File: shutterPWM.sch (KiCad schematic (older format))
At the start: 25 parts, among them P11 2x3 header strip R/A, P12 2x3 header strip R/A, U2 DRV103, U3 DRV103, U4 MCP4728

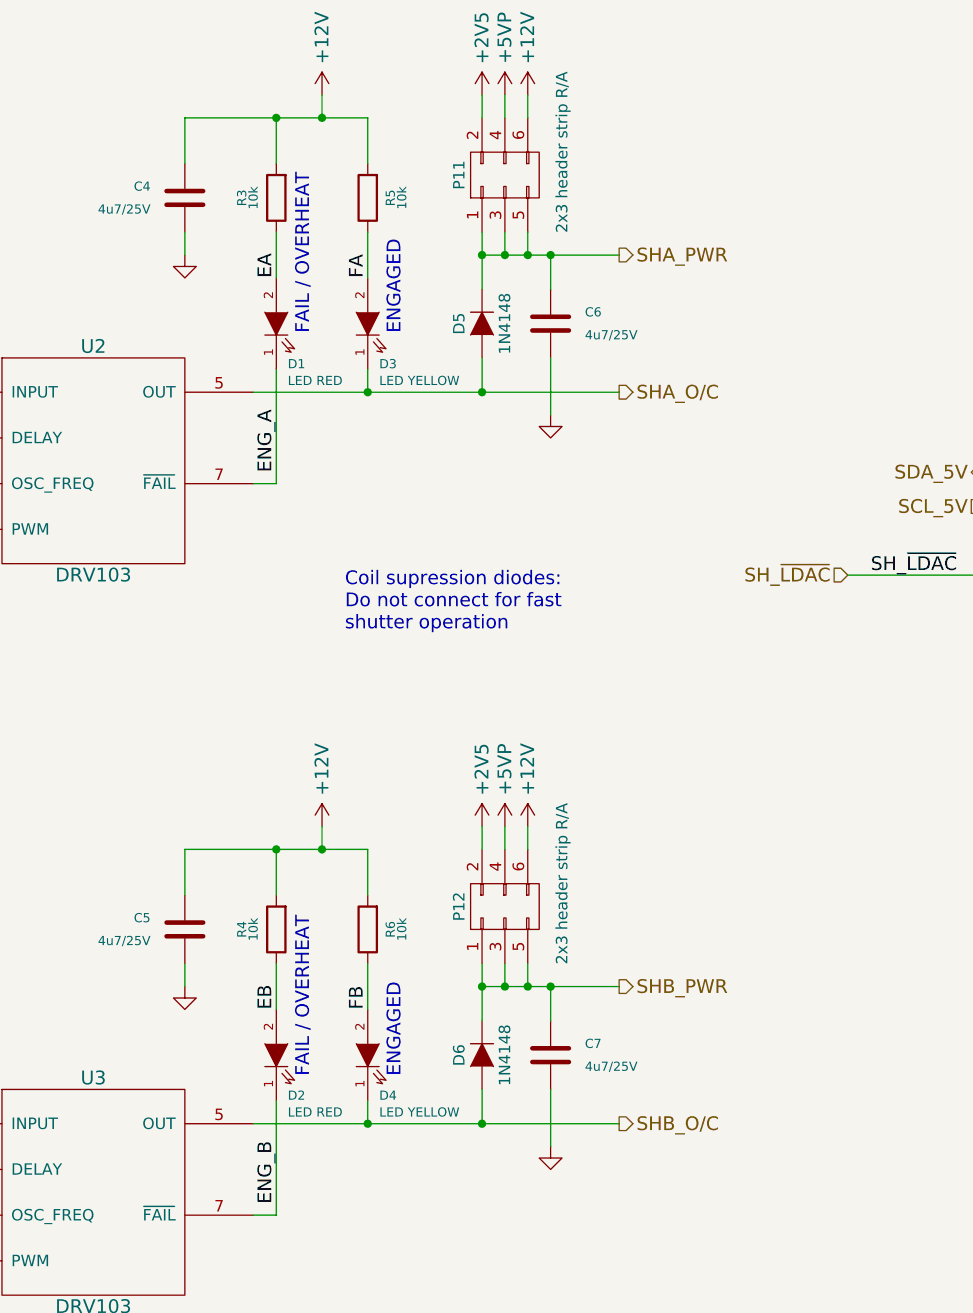
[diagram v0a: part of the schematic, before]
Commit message: Added better de-bouncing diode description
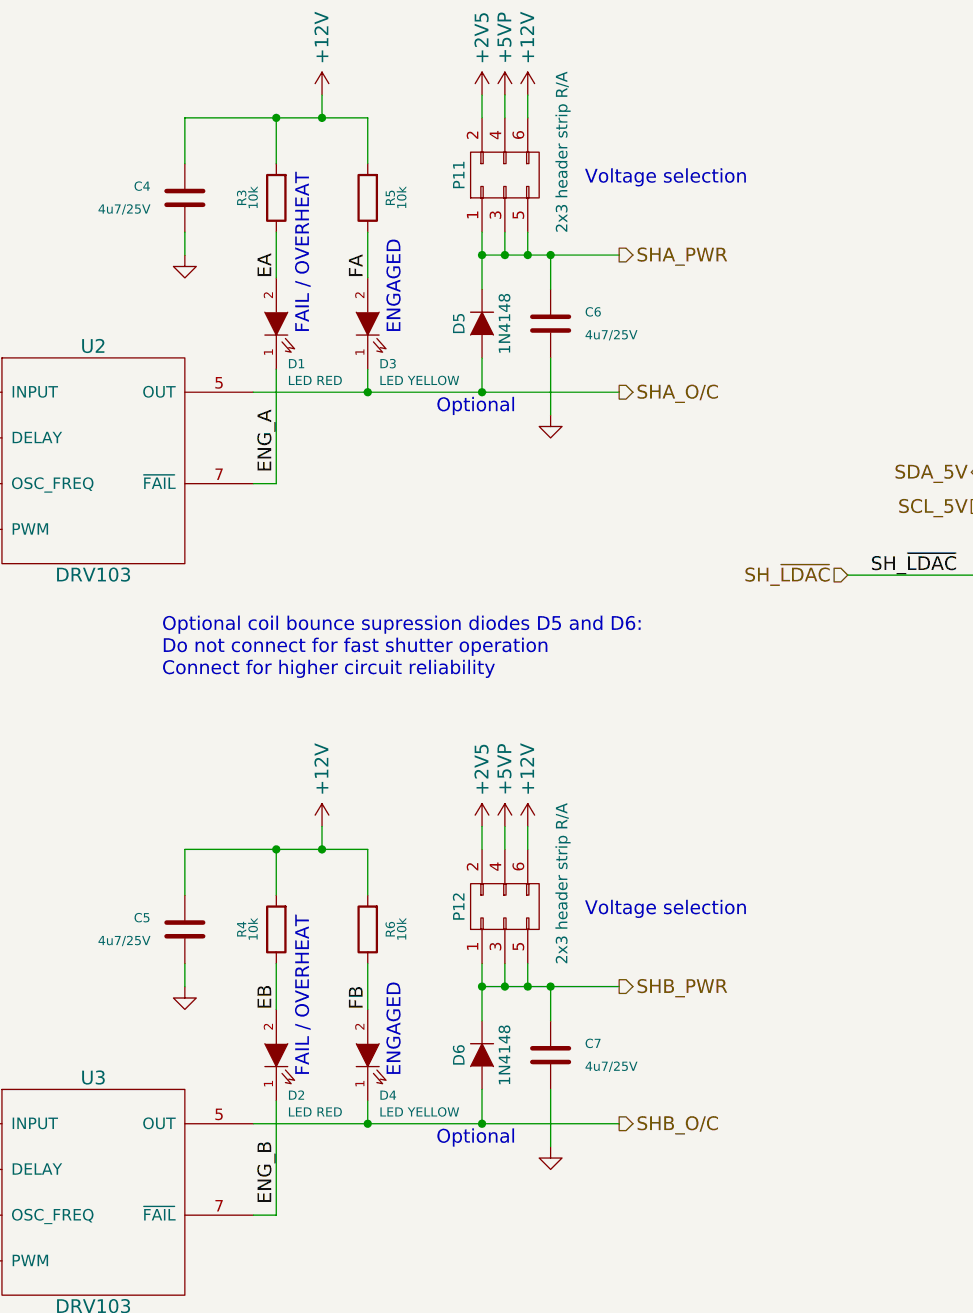
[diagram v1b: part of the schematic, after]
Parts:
- D5, D6: Note Small signal SOD-323 diode -> Optional small signal SOD-323 diode
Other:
- note added: "Optional"
- note added: "Optional coil bounce supression diodes D5 and D6:\nDo not connect for fast shutter operation\nConnect for higher circuit reliability"
- note added: "Voltage selection"
- note removed: "Coil supression diodes:\nDo not connect for fast\nshutter operation"
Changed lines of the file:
@@
 	1    0    0    -1
 $EndComp
-Text Notes 4500 3650 0    60   ~ 0
-Coil supression diodes:\nDo not connect for fast\nshutter operation
+Text Notes 3700 3850 0    60   ~ 0
+Optional coil bounce supression diodes D5 and D6:\nDo not connect for fast shutter operation\nConnect for higher circuit reliability
 $Comp
 L C C4
@@
 F 9 "Mouser" H 5100 2300 60  0001 C CNN "Alt. Supplier"
 F 10 "512-1N4148WS" H 5100 2300 60  0001 C CNN "Alt. Order Code"
-F 11 "Small signal SOD-323 diode" H 5100 2300 60  0001 C CNN "Note"
+F 11 "Optional small signal SOD-323 diode" H 5100 2300 60  0001 C CNN "Note"
 	1    5100 2300
 	0    1    1    0
@@
 F 9 "Mouser" H 5100 5500 60  0001 C CNN "Alt. Supplier"
 F 10 "512-1N4148WS" H 5100 5500 60  0001 C CNN "Alt. Order Code"
-F 11 "Small signal SOD-323 diode" H 5100 5500 60  0001 C CNN "Note"
+F 11 "Optional small signal SOD-323 diode" H 5100 5500 60  0001 C CNN "Note"
 	1    5100 5500
 	0    1    1    0
 $EndComp
+Text Notes 4900 2700 0    60   ~ 0
+Optional
+Text Notes 4900 5900 0    60   ~ 0
+Optional
+Text Notes 5550 1700 0    60   ~ 0
+Voltage selection
+Text Notes 5550 4900 0    60   ~ 0
+Voltage selection
 $EndSCHEMATC

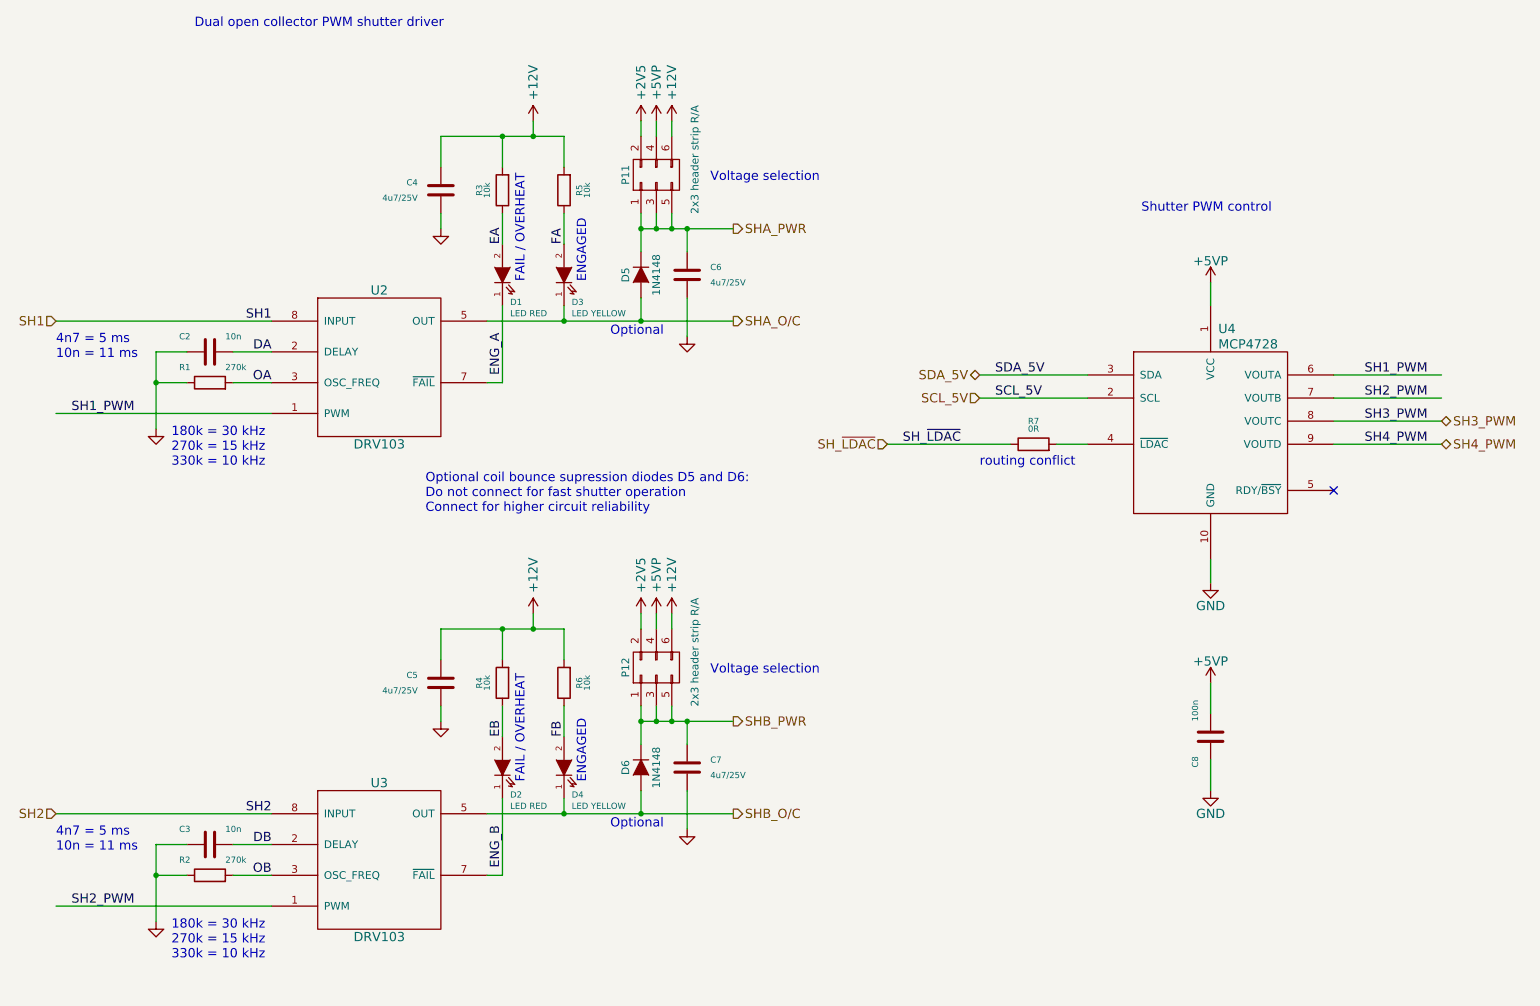
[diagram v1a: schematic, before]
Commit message: Added pullup resistors to I2C
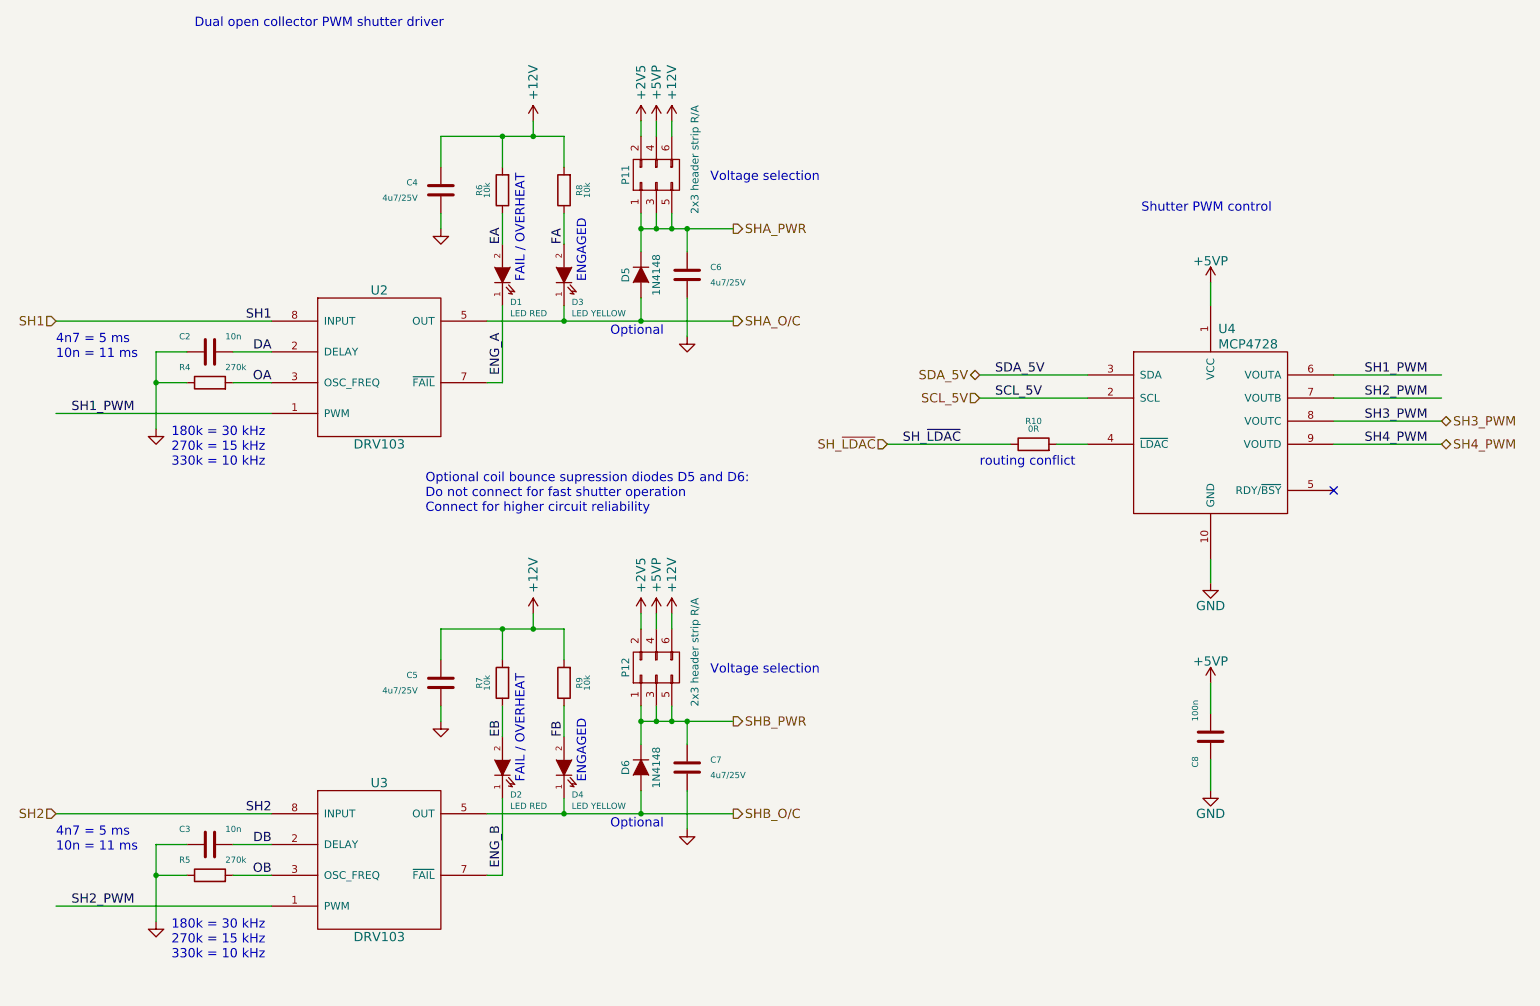
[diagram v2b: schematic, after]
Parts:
- renumbered R7 to R10, R1 to R4, R2 to R5, R3 to R6, R4 to R7, R5 to R8, R6 to R9
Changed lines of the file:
@@
 $EndComp
 $Comp
-L R R1
+L R R4
 U 1 1 53A2B9D0
 P 2300 3000
-F 0 "R1" V 2400 3200 40  0000 R CNN
+F 0 "R4" V 2400 3200 40  0000 R CNN
 F 1 "270k" V 2400 2900 40  0000 R CNN
 F 2 "Resistors_SMD:R_0805" V 2230 3000 30  0001 C CNN
@@
 $EndComp
 $Comp
-L GND #PWR015
+L GND #PWR16
 U 1 1 53A2BB0A
 P 1950 3300
-F 0 "#PWR015" H 1950 3300 30  0001 C CNN
+F 0 "#PWR16" H 1950 3300 30  0001 C CNN
 F 1 "GND" H 1950 3230 30  0001 C CNN
 F 2 "" H 1950 3300 60  0000 C CNN
@@
 $EndComp
 $Comp
-L GND #PWR016
+L GND #PWR18
 U 1 1 53A2D1AD
 P 3800 2000
-F 0 "#PWR016" H 3800 2000 30  0001 C CNN
+F 0 "#PWR18" H 3800 2000 30  0001 C CNN
 F 1 "GND" H 3800 1930 30  0001 C CNN
 F 2 "" H 3800 2000 60  0000 C CNN
@@
 4n7 = 5 ms\n10n = 11 ms
 $Comp
-L +2V5 #PWR017
+L +2V5 #PWR22
 U 1 1 554638F4
 P 5100 1300
-F 0 "#PWR017" H 5100 1150 60  0001 C CNN
+F 0 "#PWR22" H 5100 1150 60  0001 C CNN
 F 1 "+2V5" V 5100 1550 60  0000 C CNN
 F 2 "" H 5100 1300 60  0000 C CNN
@@
 SHA_O/C
 $Comp
-L +5VP #PWR018
+L +5VP #PWR24
 U 1 1 55463911
 P 5200 1300
-F 0 "#PWR018" H 5200 1150 60  0001 C CNN
+F 0 "#PWR24" H 5200 1150 60  0001 C CNN
 F 1 "+5VP" V 5200 1550 60  0000 C CNN
 F 2 "" H 5200 1300 60  0000 C CNN
@@
 $EndComp
 $Comp
-L +12V #PWR019
+L +12V #PWR26
 U 1 1 55463917
 P 5300 1300
-F 0 "#PWR019" H 5300 1150 60  0001 C CNN
+F 0 "#PWR26" H 5300 1150 60  0001 C CNN
 F 1 "+12V" V 5300 1550 60  0000 C CNN
 F 2 "" H 5300 1300 60  0000 C CNN
@@
 	5400 2450 5400 2700
 $Comp
-L GND #PWR020
+L GND #PWR28
 U 1 1 55463930
 P 5400 2700
-F 0 "#PWR020" H 5400 2700 30  0001 C CNN
+F 0 "#PWR28" H 5400 2700 30  0001 C CNN
 F 1 "GND" H 5400 2630 30  0001 C CNN
 F 2 "" H 5400 2700 60  0000 C CNN
@@
 	8800 2500 8800 2350
 $Comp
-L GND #PWR021
+L GND #PWR31
 U 1 1 55496B6C
 P 8800 4300
-F 0 "#PWR021" H 8800 4050 60  0001 C CNN
+F 0 "#PWR31" H 8800 4050 60  0001 C CNN
 F 1 "GND" H 8800 4150 60  0000 C CNN
 F 2 "" H 8800 4300 60  0000 C CNN
@@
 	8800 5450 8800 5650
 $Comp
-L GND #PWR022
+L GND #PWR33
 U 1 1 55498333
 P 8800 5650
-F 0 "#PWR022" H 8800 5400 60  0001 C CNN
+F 0 "#PWR33" H 8800 5400 60  0001 C CNN
 F 1 "GND" H 8800 5500 60  0000 C CNN
 F 2 "" H 8800 5650 60  0000 C CNN
@@
 $EndComp
 $Comp
-L R R3
+L R R6
 U 1 1 5567D385
 P 4200 1750
-F 0 "R3" V 4350 1750 40  0000 C CNN
+F 0 "R6" V 4350 1750 40  0000 C CNN
 F 1 "10k" V 4300 1750 40  0000 C CNN
 F 2 "Resistors_SMD:R_0805" V 4130 1750 30  0001 C CNN
@@
 ENGAGED
 $Comp
-L +5VP #PWR023
+L +5VP #PWR30
 U 1 1 5569B2B5
 P 8800 2350
-F 0 "#PWR023" H 8800 2200 60  0001 C CNN
+F 0 "#PWR30" H 8800 2200 60  0001 C CNN
 F 1 "+5VP" H 8800 2490 60  0000 C CNN
 F 2 "" H 8800 2350 60  0000 C CNN
@@
 $EndComp
 $Comp
-L +5VP #PWR024
+L +5VP #PWR32
 U 1 1 55697A42
 P 8800 4950
-F 0 "#PWR024" H 8800 4800 60  0001 C CNN
+F 0 "#PWR32" H 8800 4800 60  0001 C CNN
 F 1 "+5VP" H 8800 5090 60  0000 C CNN
 F 2 "" H 8800 4950 60  0000 C CNN
@@
 	4200 1400 4200 1600
 $Comp
-L +12V #PWR025
+L +12V #PWR20
 U 1 1 556A00E7
 P 4400 1300
-F 0 "#PWR025" H 4400 1150 60  0001 C CNN
+F 0 "#PWR20" H 4400 1150 60  0001 C CNN
 F 1 "+12V" V 4400 1550 60  0000 C CNN
 F 2 "" H 4400 1300 60  0000 C CNN
@@
 Connection ~ 4200 1400
 $Comp
-L GND #PWR026
+L GND #PWR17
 U 1 1 556A57C3
 P 1950 6500
-F 0 "#PWR026" H 1950 6500 30  0001 C CNN
+F 0 "#PWR17" H 1950 6500 30  0001 C CNN
 F 1 "GND" H 1950 6430 30  0001 C CNN
 F 2 "" H 1950 6500 60  0000 C CNN
@@
 $EndComp
 $Comp
-L GND #PWR027
+L GND #PWR19
 U 1 1 556A57CF
 P 3800 5200
-F 0 "#PWR027" H 3800 5200 30  0001 C CNN
+F 0 "#PWR19" H 3800 5200 30  0001 C CNN
 F 1 "GND" H 3800 5130 30  0001 C CNN
 F 2 "" H 3800 5200 60  0000 C CNN
@@
 4n7 = 5 ms\n10n = 11 ms
 $Comp
-L +2V5 #PWR028
+L +2V5 #PWR23
 U 1 1 556A57EA
 P 5100 4500
-F 0 "#PWR028" H 5100 4350 60  0001 C CNN
+F 0 "#PWR23" H 5100 4350 60  0001 C CNN
 F 1 "+2V5" V 5100 4750 60  0000 C CNN
 F 2 "" H 5100 4500 60  0000 C CNN
@@
 SHB_O/C
 $Comp
-L +5VP #PWR029
+L +5VP #PWR25
 U 1 1 556A57F2
 P 5200 4500
-F 0 "#PWR029" H 5200 4350 60  0001 C CNN
+F 0 "#PWR25" H 5200 4350 60  0001 C CNN
 F 1 "+5VP" V 5200 4750 60  0000 C CNN
 F 2 "" H 5200 4500 60  0000 C CNN
@@
 $EndComp
 $Comp
-L +12V #PWR030
+L +12V #PWR27
 U 1 1 556A57F8
 P 5300 4500
-F 0 "#PWR030" H 5300 4350 60  0001 C CNN
+F 0 "#PWR27" H 5300 4350 60  0001 C CNN
 F 1 "+12V" V 5300 4750 60  0000 C CNN
 F 2 "" H 5300 4500 60  0000 C CNN
@@
 	5400 5650 5400 5900
 $Comp
-L GND #PWR031
+L GND #PWR29
 U 1 1 556A5805
 P 5400 5900
-F 0 "#PWR031" H 5400 5900 30  0001 C CNN
+F 0 "#PWR29" H 5400 5900 30  0001 C CNN
 F 1 "GND" H 5400 5830 30  0001 C CNN
 F 2 "" H 5400 5900 60  0000 C CNN
@@
 	4200 4600 4200 4800
 $Comp
-L +12V #PWR032
+L +12V #PWR21
 U 1 1 556A5850
 P 4400 4500
-F 0 "#PWR032" H 4400 4350 60  0001 C CNN
+F 0 "#PWR21" H 4400 4350 60  0001 C CNN
 F 1 "+12V" V 4400 4750 60  0000 C CNN
 F 2 "" H 4400 4500 60  0000 C CNN
@@
 	6700 3400 7500 3400
 $Comp
-L R R2
+L R R5
 U 1 1 55C0F844
 P 2300 6200
-F 0 "R2" V 2400 6400 40  0000 R CNN
+F 0 "R5" V 2400 6400 40  0000 R CNN
 F 1 "270k" V 2400 6100 40  0000 R CNN
 F 2 "Resistors_SMD:R_0805" V 2230 6200 30  0001 C CNN
@@
 $EndComp
 $Comp
-L R R5
+L R R8
 U 1 1 55C104F3
 P 4600 1750
-F 0 "R5" V 4500 1750 40  0000 C CNN
+F 0 "R8" V 4500 1750 40  0000 C CNN
 F 1 "10k" V 4450 1750 40  0000 C CNN
 F 2 "Resistors_SMD:R_0805" V 4530 1750 30  0001 C CNN
@@
 $EndComp
 $Comp
-L R R4
+L R R7
 U 1 1 55C10AA5
 P 4200 4950
-F 0 "R4" V 4350 4950 40  0000 C CNN
+F 0 "R7" V 4350 4950 40  0000 C CNN
 F 1 "10k" V 4300 4950 40  0000 C CNN
 F 2 "Resistors_SMD:R_0805" V 4130 4950 30  0001 C CNN
@@
 $EndComp
 $Comp
-L R R6
+L R R9
 U 1 1 55C10BB7
 P 4600 4950
-F 0 "R6" V 4500 4950 40  0000 C CNN
+F 0 "R9" V 4500 4950 40  0000 C CNN
 F 1 "10k" V 4450 4950 40  0000 C CNN
 F 2 "Resistors_SMD:R_0805" V 4530 4950 30  0001 C CNN
@@
 $EndComp
 $Comp
-L R R7
+L R R10
 U 1 1 55C2DF41
 P 7650 3400
-F 0 "R7" V 7800 3400 40  0000 C CNN
+F 0 "R10" V 7800 3400 40  0000 C CNN
 F 1 "0R" V 7750 3400 40  0000 C CNN
 F 2 "Resistors_SMD:R_0805" V 7580 3400 30  0001 C CNN
